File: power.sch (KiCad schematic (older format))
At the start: 23 parts

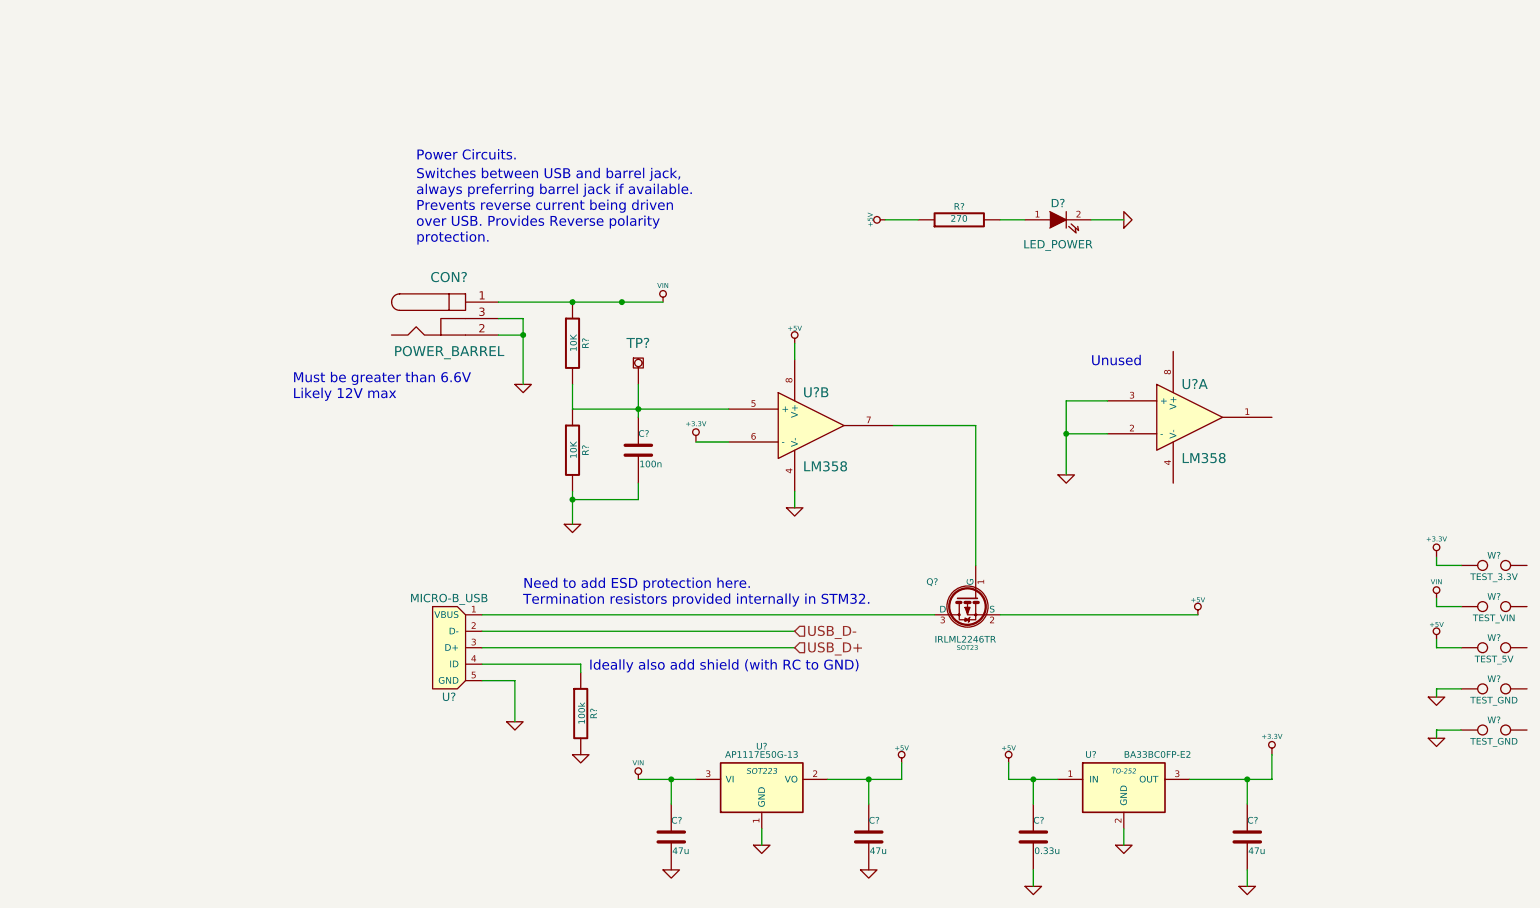
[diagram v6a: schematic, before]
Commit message: DRCs mostly fixed
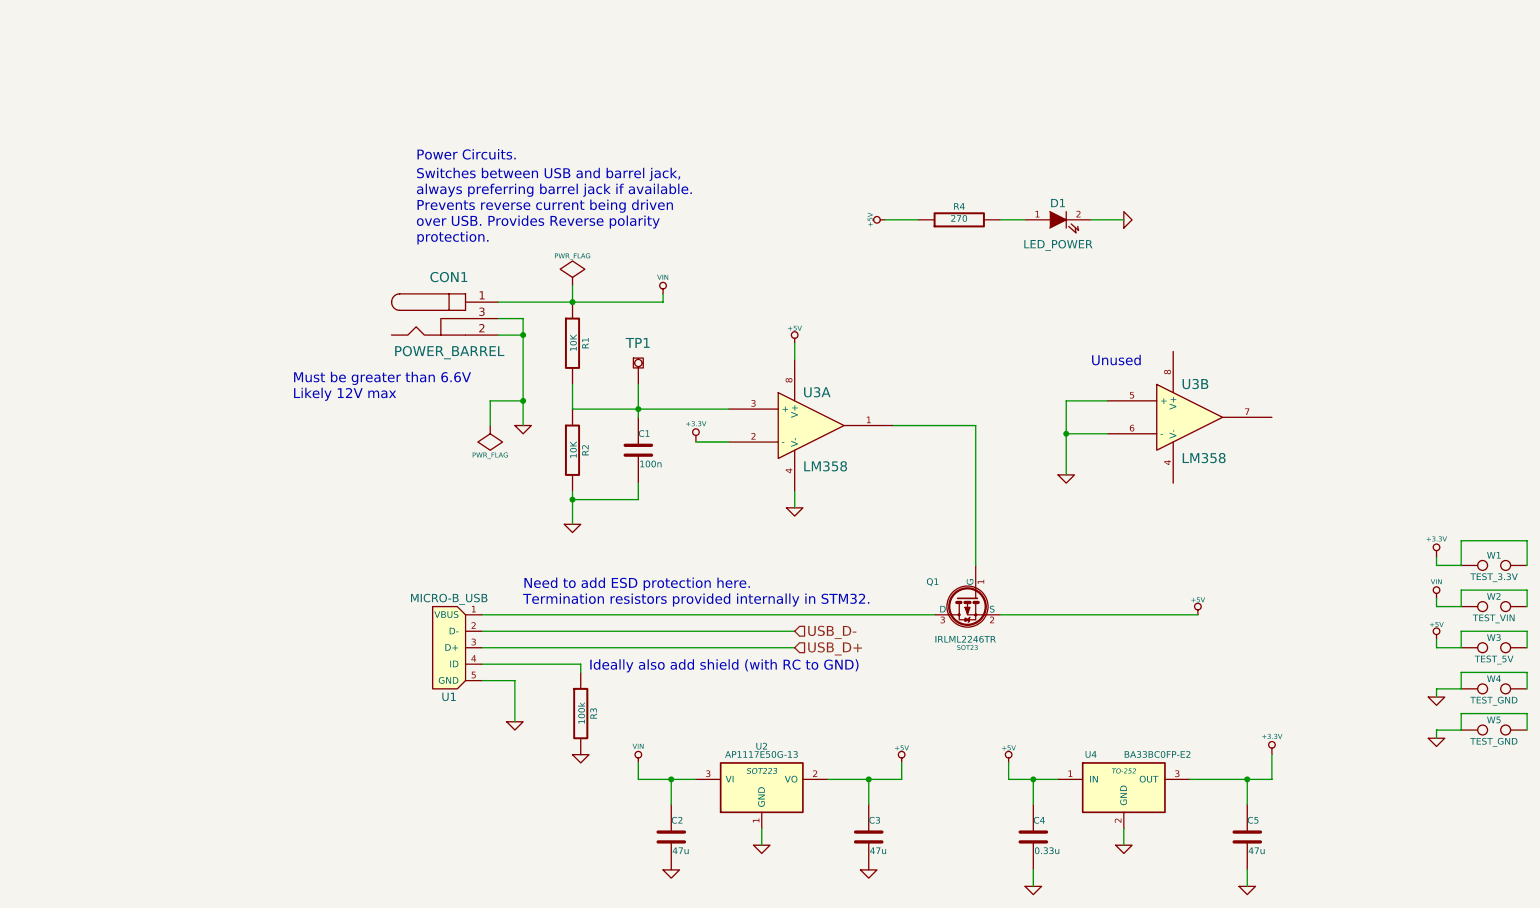
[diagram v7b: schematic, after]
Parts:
- gave numbers to parts that had none: 22
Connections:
- net +3.3V: now also U3.2 (-), W1.2; no longer U3.6 (-)
- net +5V: now also W3.2
- net GND: now also U3.5 (+), U3.6 (-), W4.2, W5.2; no longer U3.2 (-), U3.3 (+)
- net VIN: now also W2.2
- net at C1.1, R1.2, R2.1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: now also U3.3 (+); no longer U3.5 (+)
- net at Q1.1 (G): now also U3.1; no longer U3.7
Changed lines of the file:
@@
 $EndDescr
 $Comp
-L BARREL_JACK CON?
+L BARREL_JACK CON1
 U 1 1 5566063A
 P 3500 2450
-F 0 "CON?" H 3500 2700 60  0000 C CNN
+F 0 "CON1" H 3500 2700 60  0000 C CNN
 F 1 "POWER_BARREL" H 3500 2250 60  0000 C CNN
 F 2 "" H 3500 2450 60  0000 C CNN
@@
 $EndComp
 $Comp
-L MICRO-B_USB U?
+L MICRO-B_USB U1
 U 1 1 55660641
 P 3500 4450
-F 0 "U?" H 3500 4150 50  0000 C CNN
+F 0 "U1" H 3500 4150 50  0000 C CNN
 F 1 "MICRO-B_USB" H 3500 4750 50  0000 C CNN
 F 2 "" H 3500 4450 60  0000 C CNN
@@
 $EndComp
 $Comp
-L BA33BC0FP-E2 U?
+L BA33BC0FP-E2 U4
 U 1 1 55660648
 P 7600 5300
-F 0 "U?" H 7400 5500 40  0000 C CNN
+F 0 "U4" H 7400 5500 40  0000 C CNN
 F 1 "BA33BC0FP-E2" H 7600 5500 40  0000 L CNN
 F 2 "TO-252" H 7600 5400 30  0000 C CIN
@@
 $EndComp
 $Comp
-L LED D?
+L LED D1
 U 1 1 55660A5B
 P 7200 1850
-F 0 "D?" H 7200 1950 50  0000 C CNN
+F 0 "D1" H 7200 1950 50  0000 C CNN
 F 1 "LED_POWER" H 7200 1700 50  0000 C CNN
 F 2 "" H 7200 1850 60  0000 C CNN
@@
 $EndComp
 $Comp
-L AP1117E50G-13 U?
+L AP1117E50G-13 U2
 U 1 1 55660BBD
 P 5400 5300
-F 0 "U?" H 5400 5550 40  0000 C CNN
+F 0 "U2" H 5400 5550 40  0000 C CNN
 F 1 "AP1117E50G-13" H 5400 5500 40  0000 C CNN
 F 2 "SOT223" H 5400 5400 35  0000 C CIN
@@
 $EndComp
 $Comp
-L LM358 U?
-U 1 1 55660C3A
+L LM358 U3
+U 2 1 55660C3A
 P 8000 3050
-F 0 "U?" H 7950 3250 60  0000 L CNN
+F 0 "U3" H 7950 3250 60  0000 L CNN
 F 1 "LM358" H 7950 2800 60  0000 L CNN
 F 2 "" H 8000 3050 60  0000 C CNN
 F 3 "" H 8000 3050 60  0000 C CNN
-	1    8000 3050
-	1    0    0    -1
-$EndComp
-$Comp
-L LM358 U?
-U 2 1 55660DA5
+	2    8000 3050
+	1    0    0    -1
+$EndComp
+$Comp
+L LM358 U3
+U 1 1 55660DA5
 P 5700 3100
-F 0 "U?" H 5650 3300 60  0000 L CNN
+F 0 "U3" H 5650 3300 60  0000 L CNN
 F 1 "LM358" H 5650 2850 60  0000 L CNN
 F 2 "" H 5700 3100 60  0000 C CNN
 F 3 "" H 5700 3100 60  0000 C CNN
-	2    5700 3100
-	1    0    0    -1
-$EndComp
-$Comp
-L IRLML2246TR Q?
+	1    5700 3100
+	1    0    0    -1
+$EndComp
+$Comp
+L IRLML2246TR Q1
 U 1 1 5566119A
 P 6650 4150
-F 0 "Q?" V 6550 4400 40  0000 R CNN
+F 0 "Q1" V 6550 4400 40  0000 R CNN
 F 1 "IRLML2246TR" V 6900 4350 40  0000 R CNN
 F 2 "SOT23" V 6950 4150 29  0000 C CNN
@@
 Switches between USB and barrel jack,\nalways preferring barrel jack if available.\nPrevents reverse current being driven\nover USB. Provides Reverse polarity \nprotection.
 $Comp
-L R R?
+L R R1
 U 1 1 55661576
 P 4250 2600
-F 0 "R?" V 4330 2600 40  0000 C CNN
+F 0 "R1" V 4330 2600 40  0000 C CNN
 F 1 "10K" V 4257 2601 40  0000 C CNN
 F 2 "" V 4180 2600 30  0000 C CNN
@@
 $EndComp
 $Comp
-L R R?
+L R R2
 U 1 1 55661616
 P 4250 3250
-F 0 "R?" V 4330 3250 40  0000 C CNN
+F 0 "R2" V 4330 3250 40  0000 C CNN
 F 1 "10K" V 4257 3251 40  0000 C CNN
 F 2 "" V 4180 3250 30  0000 C CNN
@@
 $EndComp
 $Comp
-L C C?
+L C C1
 U 1 1 55661649
 P 4650 3250
-F 0 "C?" H 4650 3350 40  0000 L CNN
+F 0 "C1" H 4650 3350 40  0000 L CNN
 F 1 "100n" H 4656 3165 40  0000 L CNN
 F 2 "" H 4688 3100 30  0000 C CNN
@@
 L GND #PWR03
 U 1 1 556622F1
-P 3950 2850
-F 0 "#PWR03" H 3950 2850 30  0001 C CNN
-F 1 "GND" H 3950 2780 30  0001 C CNN
-F 2 "" H 3950 2850 60  0000 C CNN
-F 3 "" H 3950 2850 60  0000 C CNN
-	1    3950 2850
+P 3950 3100
+F 0 "#PWR03" H 3950 3100 30  0001 C CNN
+F 1 "GND" H 3950 3030 30  0001 C CNN
+F 2 "" H 3950 3100 60  0000 C CNN
+F 3 "" H 3950 3100 60  0000 C CNN
+	1    3950 3100
 	1    0    0    -1
 $EndComp
@@
 $EndComp
 $Comp
-L R R?
+L R R4
 U 1 1 55662F52
 P 6600 1850
-F 0 "R?" V 6680 1850 40  0000 C CNN
+F 0 "R4" V 6680 1850 40  0000 C CNN
 F 1 "270" V 6607 1851 40  0000 C CNN
 F 2 "" V 6530 1850 30  0000 C CNN
@@
 $EndComp
 $Comp
-L C C?
+L C C2
 U 1 1 5566535A
 P 4850 5600
-F 0 "C?" H 4850 5700 40  0000 L CNN
+F 0 "C2" H 4850 5700 40  0000 L CNN
 F 1 "47u" H 4856 5515 40  0000 L CNN
 F 2 "" H 4888 5450 30  0000 C CNN
@@
 	3800 2550 3950 2550
 Wire Wire Line
-	3950 2450 3950 2850
+	3950 2450 3950 3100
 Wire Wire Line
 	3800 2450 3950 2450
@@
 Wire Wire Line
 	3800 2350 4800 2350
-Connection ~ 4550 2350
 $Comp
 L GND #PWR016
@@
 Connection ~ 4850 5250
 $Comp
-L C C?
+L C C3
 U 1 1 55665905
 P 6050 5600
-F 0 "C?" H 6050 5700 40  0000 L CNN
+F 0 "C3" H 6050 5700 40  0000 L CNN
 F 1 "47u" H 6056 5515 40  0000 L CNN
 F 2 "" H 6088 5450 30  0000 C CNN
@@
 $EndComp
 $Comp
-L C C?
+L C C5
 U 1 1 55665B22
 P 8350 5600
-F 0 "C?" H 8350 5700 40  0000 L CNN
+F 0 "C5" H 8350 5700 40  0000 L CNN
 F 1 "47u" H 8356 5515 40  0000 L CNN
 F 2 "" H 8388 5450 30  0000 C CNN
@@
 	8350 5800 8350 5900
 $Comp
-L C C?
+L C C4
 U 1 1 55665C0A
 P 7050 5600
-F 0 "C?" H 7050 5700 40  0000 L CNN
+F 0 "C4" H 7050 5700 40  0000 L CNN
 F 1 "0.33u" H 7056 5515 40  0000 L CNN
 F 2 "" H 7088 5450 30  0000 C CNN
@@
 	1    0    0    -1
 $EndComp
-Wire Wire Line
-	7050 5800 7050 5900
 Text Notes 2550 2950 0    60   ~ 0
 Must be greater than 6.6V\nLikely 12V max
@@
 USB_D+
 $Comp
-L TEST W?
+L TEST W4
 U 1 1 55675FE3
 P 9850 4700
-F 0 "W?" H 9850 4760 40  0000 C CNN
+F 0 "W4" H 9850 4760 40  0000 C CNN
 F 1 "TEST_GND" H 9850 4630 40  0000 C CNN
 F 2 "" H 9850 4700 60  0000 C CNN
@@
 $EndComp
 $Comp
-L TEST W?
+L TEST W5
 U 1 1 55675FEA
 P 9850 4950
-F 0 "W?" H 9850 5010 40  0000 C CNN
+F 0 "W5" H 9850 5010 40  0000 C CNN
 F 1 "TEST_GND" H 9850 4880 40  0000 C CNN
 F 2 "" H 9850 4950 60  0000 C CNN
@@
 $EndComp
 $Comp
-L TEST W?
+L TEST W1
 U 1 1 55675FF1
 P 9850 3950
-F 0 "W?" H 9850 4010 40  0000 C CNN
+F 0 "W1" H 9850 4010 40  0000 C CNN
 F 1 "TEST_3.3V" H 9850 3880 40  0000 C CNN
 F 2 "" H 9850 3950 60  0000 C CNN
@@
 $EndComp
 $Comp
-L TEST W?
+L TEST W2
 U 1 1 55675FF8
 P 9850 4200
-F 0 "W?" H 9850 4260 40  0000 C CNN
+F 0 "W2" H 9850 4260 40  0000 C CNN
 F 1 "TEST_VIN" H 9850 4130 40  0000 C CNN
 F 2 "" H 9850 4200 60  0000 C CNN
@@
 	9500 4700 9650 4700
 $Comp
-L TEST W?
+L TEST W3
 U 1 1 5567647D
 P 9850 4450
-F 0 "W?" H 9850 4510 40  0000 C CNN
+F 0 "W3" H 9850 4510 40  0000 C CNN
 F 1 "TEST_5V" H 9850 4380 40  0000 C CNN
 F 2 "" H 9850 4450 60  0000 C CNN
@@
 L VIN #PWR025
 U 1 1 5567710F
-P 4800 2350
-F 0 "#PWR025" H 4800 2450 30  0001 C CNN
-F 1 "VIN" H 4800 2450 30  0000 C CNN
-F 2 "" H 4800 2350 60  0000 C CNN
-F 3 "" H 4800 2350 60  0000 C CNN
-	1    4800 2350
+P 4800 2300
+F 0 "#PWR025" H 4800 2400 30  0001 C CNN
+F 1 "VIN" H 4800 2400 30  0000 C CNN
+F 2 "" H 4800 2300 60  0000 C CNN
+F 3 "" H 4800 2300 60  0000 C CNN
+	1    4800 2300
 	1    0    0    -1
 $EndComp
@@
 L VIN #PWR026
 U 1 1 556772F1
-P 4650 5250
-F 0 "#PWR026" H 4650 5350 30  0001 C CNN
-F 1 "VIN" H 4650 5350 30  0000 C CNN
-F 2 "" H 4650 5250 60  0000 C CNN
-F 3 "" H 4650 5250 60  0000 C CNN
-	1    4650 5250
+P 4650 5150
+F 0 "#PWR026" H 4650 5250 30  0001 C CNN
+F 1 "VIN" H 4650 5250 30  0000 C CNN
+F 2 "" H 4650 5150 60  0000 C CNN
+F 3 "" H 4650 5150 60  0000 C CNN
+	1    4650 5150
 	1    0    0    -1
 $EndComp
@@
 	4300 4550 4300 4600
 $Comp
-L R R?
+L R R3
 U 1 1 55678D89
 P 4300 4850
-F 0 "R?" V 4380 4850 40  0000 C CNN
+F 0 "R3" V 4380 4850 40  0000 C CNN
 F 1 "100k" V 4307 4851 40  0000 C CNN
 F 2 "" V 4230 4850 30  0000 C CNN
@@
 Ideally also add shield (with RC to GND)
 $Comp
-L TESTPOINT TP?
+L TESTPOINT TP1
 U 1 1 556C2967
 P 4650 2850
-F 0 "TP?" H 4650 3100 60  0000 C CNN
+F 0 "TP1" H 4650 3100 60  0000 C CNN
 F 1 "TESTPOINT" H 4650 2800 60  0001 C CNN
 F 2 "" H 4650 2850 60  0000 C CNN
@@
 	1    0    0    -1
 $EndComp
+Wire Wire Line
+	9650 3950 9650 3800
+Wire Wire Line
+	9650 3800 10050 3800
+Wire Wire Line
+	10050 3800 10050 3950
+Wire Wire Line
+	9650 4200 9650 4100
+Wire Wire Line
+	9650 4100 10050 4100
+Wire Wire Line
+	10050 4100 10050 4200
+Wire Wire Line
+	9650 4450 9650 4350
+Wire Wire Line
+	9650 4350 10050 4350
+Wire Wire Line
+	10050 4350 10050 4450
+Wire Wire Line
+	9650 4700 9650 4600
+Wire Wire Line
+	9650 4600 10050 4600
+Wire Wire Line
+	10050 4600 10050 4700
+Wire Wire Line
+	9650 4950 9650 4850
+Wire Wire Line
+	9650 4850 10050 4850
+Wire Wire Line
+	10050 4850 10050 4950
+Wire Wire Line
+	7050 5800 7050 5900
+Wire Wire Line
+	4650 5150 4650 5250
+Wire Wire Line
+	4800 2350 4800 2300
+$Comp
+L PWR_FLAG #FLG028
+U 1 1 556C9294
+P 4250 2250
+F 0 "#FLG028" H 4250 2345 30  0001 C CNN
+F 1 "PWR_FLAG" H 4250 2430 30  0000 C CNN
+F 2 "" H 4250 2250 60  0000 C CNN
+F 3 "" H 4250 2250 60  0000 C CNN
+	1    4250 2250
+	1    0    0    -1
+$EndComp
+$Comp
+L PWR_FLAG #FLG029
+U 1 1 556C9325
+P 3750 3100
+F 0 "#FLG029" H 3750 3195 30  0001 C CNN
+F 1 "PWR_FLAG" H 3750 3280 30  0000 C CNN
+F 2 "" H 3750 3100 60  0000 C CNN
+F 3 "" H 3750 3100 60  0000 C CNN
+	1    3750 3100
+	-1   0    0    1
+$EndComp
+Wire Wire Line
+	3750 3100 3750 2950
+Wire Wire Line
+	3750 2950 3950 2950
+Connection ~ 3950 2950
+Wire Wire Line
+	4250 2250 4250 2350
 $EndSCHEMATC

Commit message: Start routing
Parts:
- removed W1: TEST_3.3V, symbol TEST
- removed W2: TEST_VIN, symbol TEST
- removed W3: TEST_5V, symbol TEST
- removed W4, W5: TEST_GND, symbol TEST
- added TP11, TP12, TP13, TP14, TP15: TESTPOINT, Connect:TESTPOINT, symbol TESTPOINT
- C1, C4: footprint (none) -> Capacitors_SMD:C_0603_HandSoldering
- C2, C3, C5: footprint (none) -> Capacitors_SMD:c_elec_8x6.5
- CON1: footprint (none) -> Connect:BARREL_JACK
- D1: footprint (none) -> LEDs:LED-0603
- Q1: footprint SOT23 -> SOT23_Transistor_RevA_03Aug2010:SOT23_Transistor_Handsoldering_RevA_03Aug2010
- R1, R2, R3, R4: footprint (none) -> Resistors_SMD:R_0603_HandSoldering
- TP1: footprint (none) -> Connect:PINTST
- U1: footprint (none) -> Connect:USB_Micro-B
- U2: footprint SOT223 -> SOT223:SOT223
- U3: footprint (none) -> Housings_SOIC:SOIC-8-1EP_3.9x4.9mm_Pitch1.27mm
- U4: footprint TO-252 -> ok-smd-generic:TO-252
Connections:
- net +3.3V: now also TP11.1
- net +5V: now also TP13.1
- net GND: now also TP14.1, TP15.1
- net VIN: now also TP12.1
